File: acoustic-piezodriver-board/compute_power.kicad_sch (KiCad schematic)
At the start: 29 parts, among them J301 Conn_02x06_Odd_Even, U10 NCE6005AS, U302 TMCS1108A3UQDR, U9 LM3478MM

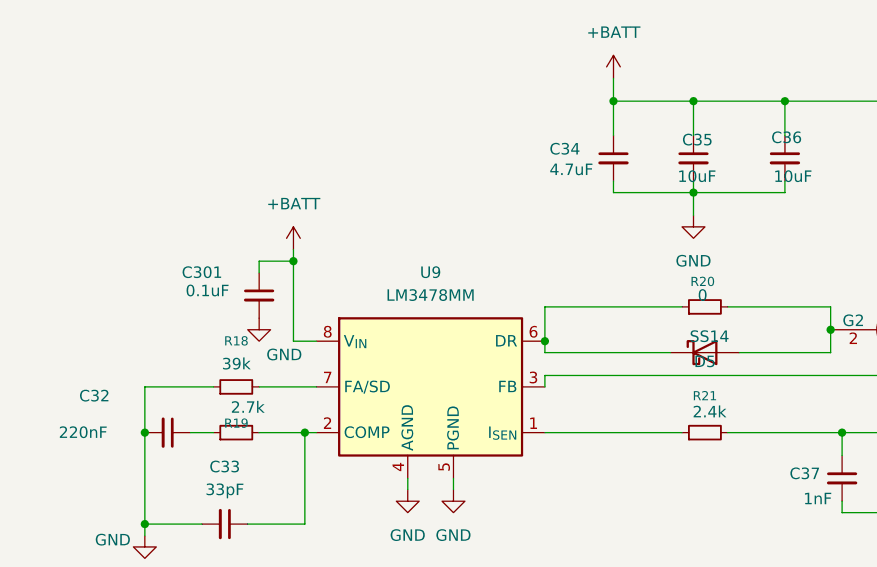
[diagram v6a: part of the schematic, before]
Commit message: Fixed ERC, DRC errors, finished routing (next) perform footprint checks
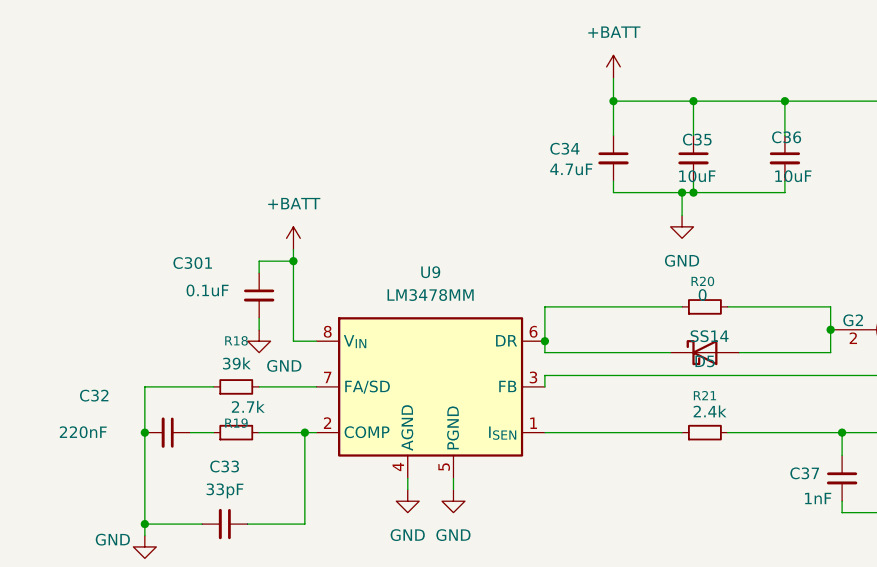
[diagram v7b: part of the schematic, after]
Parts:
- C301: footprint Capacitor_SMD:C_0201_0603Metric -> Capacitor_SMD:C_0402_1005Metric; LPN C22435929 -> C307331; MPN CGA0201X7R104K160ET -> CL05B104KB54PNC
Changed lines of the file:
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@@
 	)
 	(junction
-		(at 241.3 72.39)
+		(at 240.03 72.39)
 		(diameter 0)
 		(color 0 0 0 0)
@@
 	)
 	(junction
+		(at 241.3 72.39)
+		(diameter 0)
+		(color 0 0 0 0)
+	)
+	(junction
 		(at 50.8 62.23)
 		(diameter 0)
@@
 	(wire
 		(pts
+			(xy 193.04 87.63) (xy 193.04 86.36)
+		)
+		(stroke
+			(width 0)
+			(type default)
+		)
+	)
+	(wire
+		(pts
 			(xy 285.75 107.95) (xy 285.75 104.14)
 		)
@@
 	(wire
 		(pts
-			(xy 241.3 74.93) (xy 241.3 72.39)
+			(xy 240.03 74.93) (xy 240.03 72.39)
 		)
 		(stroke
@@
 	(wire
 		(pts
+			(xy 241.3 72.39) (xy 251.46 72.39)
+		)
+		(stroke
+			(width 0)
+			(type default)
+		)
+	)
+	(wire
+		(pts
 			(xy 45.72 140.97) (xy 45.72 135.89)
 		)
@@
 	(wire
 		(pts
-			(xy 232.41 72.39) (xy 241.3 72.39)
+			(xy 232.41 72.39) (xy 240.03 72.39)
 		)
 		(stroke
@@
 	(wire
 		(pts
-			(xy 241.3 72.39) (xy 251.46 72.39)
+			(xy 240.03 72.39) (xy 241.3 72.39)
 		)
 		(stroke
@@
 	(symbol
 		(lib_id "power:GND")
-		(at 193.04 86.36 0)
+		(at 193.04 87.63 0)
 		(unit 1)
 		(exclude_from_sim no)
@@
 		(dnp no)
 		(property "Reference" "#PWR0302"
-			(at 193.04 92.71 0)
+			(at 193.04 93.98 0)
 			(effects
 				(font
@@
 		)
 		(property "Value" "GND"
-			(at 195.834 90.424 0)
+			(at 195.834 91.694 0)
 			(effects
 				(font
@@
 		)
 		(property "Footprint" ""
-			(at 193.04 86.36 0)
+			(at 193.04 87.63 0)
 			(effects
 				(font
@@
 		)
 		(property "Datasheet" ""
-			(at 193.04 86.36 0)
+			(at 193.04 87.63 0)
 			(effects
 				(font
@@
 		)
 		(property "Description" "Power symbol creates a global label with name \"GND\" , ground"
-			(at 193.04 86.36 0)
+			(at 193.04 87.63 0)
 			(effects
 				(font
@@
 	)
 	(symbol
-		(lib_id "Device:C_Small")
-		(at 193.04 83.82 0)
-		(mirror y)
-		(unit 1)
-		(exclude_from_sim no)
-		(in_bom yes)
-		(on_board yes)
-		(dnp no)
-		(property "Reference" "C301"
-			(at 188.976 81.28 0)
-			(effects
-				(font
-					(size 1.27 1.27)
-				)
-				(justify left)
-			)
-		)
-		(property "Value" "0.1uF"
-			(at 189.738 83.312 0)
-			(effects
-				(font
-					(size 1.27 1.27)
-				)
-				(justify left)
-			)
-		)
-		(property "Footprint" "Capacitor_SMD:C_0201_0603Metric"
-			(at 193.04 83.82 0)
-			(effects
-				(font
-					(size 1.27 1.27)
-				)
-				(hide yes)
-			)
-		)
-		(property "Datasheet" "https://jlcpcb.com/api/file/downloadByFileSystemAccessId/8603345729432014848"
-			(at 193.04 83.82 0)
-			(effects
-				(font
-					(size 1.27 1.27)
-				)
-				(hide yes)
-			)
-		)
-		(property "Description" "Unpolarized capacitor, small symbol"
-			(at 193.04 83.82 0)
-			(effects
-				(font
-					(size 1.27 1.27)
-				)
-				(hide yes)
-			)
-		)
-		(property "LPN" "C22435929"
-			(at 193.04 83.82 0)
-			(effects
-				(font
-					(size 1.27 1.27)
-				)
-				(hide yes)
-			)
-		)
-		(property "MPN" "CGA0201X7R104K160ET "
-			(at 193.04 83.82 0)
-			(effects
-				(font
-					(size 1.27 1.27)
-				)
-				(hide yes)
-			)
-		)
-		(property "Availability" ""
-			(at 193.04 83.82 0)
-			(effects
-				(font
-					(size 1.27 1.27)
-				)
-				(hide yes)
-			)
-		)
-		(property "Check_prices" ""
-			(at 193.04 83.82 0)
-			(effects
-				(font
-					(size 1.27 1.27)
-				)
-				(hide yes)
-			)
-		)
-		(pin "2"
-		)
-		(pin "1"
-		)
-		(instances
-			(project "acoustic-piezodriver-board"
-				(path "/94cb090f-214e-44cc-b8ed-ae50ff29d2bf/a0fbc78d-8163-4e6b-8d81-98a3dd6573cb"
-					(reference "C301")
-					(unit 1)
-				)
-			)
-		)
-	)
-	(symbol
 		(lib_id "power:GND")
 		(at 40.64 129.54 0)
@@
 	(symbol
 		(lib_id "power:GND")
-		(at 241.3 74.93 0)
+		(at 240.03 74.93 0)
 		(unit 1)
 		(exclude_from_sim no)
@@
 		(fields_autoplaced yes)
 		(property "Reference" "#PWR042"
-			(at 241.3 81.28 0)
+			(at 240.03 81.28 0)
 			(effects
 				(font
@@
 		)
 		(property "Value" "GND"
-			(at 241.3 80.01 0)
+			(at 240.03 80.01 0)
 			(effects
 				(font
@@
 		)
 		(property "Footprint" ""
-			(at 241.3 74.93 0)
+			(at 240.03 74.93 0)
 			(effects
 				(font
@@
 		)
 		(property "Datasheet" ""
-			(at 241.3 74.93 0)
+			(at 240.03 74.93 0)
 			(effects
 				(font
@@
 		)
 		(property "Description" "Power symbol creates a global label with name \"GND\" , ground"
-			(at 241.3 74.93 0)
+			(at 240.03 74.93 0)
 			(effects
 				(font
@@
 					(unit 1)
 				)
+			)
+		)
+	)
+	(symbol
+		(lib_id "Device:C_Small")
+		(at 193.04 83.82 0)
+		(mirror y)
+		(unit 1)
+		(exclude_from_sim no)
+		(in_bom yes)
+		(on_board yes)
+		(dnp no)
+		(property "Reference" "C301"
+			(at 187.96 80.264 0)
+			(effects
+				(font
+					(size 1.27 1.27)
+				)
+				(justify left)
+			)
+		)
+		(property "Value" "0.1uF"
+			(at 189.738 83.312 0)
+			(effects
+				(font
+					(size 1.27 1.27)
+				)
+				(justify left)
+			)
+		)
+		(property "Footprint" "Capacitor_SMD:C_0402_1005Metric"
+			(at 193.04 83.82 0)
+			(effects
+				(font
+					(size 1.27 1.27)
+				)
+				(hide yes)
+			)
+		)
+		(property "Datasheet" "https://jlcpcb.com/api/file/downloadByFileSystemAccessId/8603345729432014848"
+			(at 193.04 83.82 0)
+			(effects
+				(font
+					(size 1.27 1.27)
+				)
+				(hide yes)
+			)
+		)
+		(property "Description" "Unpolarized capacitor, small symbol"
+			(at 193.04 83.82 0)
+			(effects
+				(font
+					(size 1.27 1.27)
+				)
+				(hide yes)
+			)
+		)
+		(property "LPN" "C307331"
+			(at 193.04 83.82 0)
+			(effects
+				(font
+					(size 1.27 1.27)
+				)
+				(hide yes)
+			)
+		)
+		(property "MPN" "CL05B104KB54PNC"
+			(at 193.04 83.82 0)
+			(effects
+				(font
+					(size 1.27 1.27)
+				)
+				(hide yes)
+			)
+		)
+		(pin "2"
+		)
+		(pin "1"
+		)
+		(instances
+			(project "acoustic-piezodriver-board"
+				(path "/94cb090f-214e-44cc-b8ed-ae50ff29d2bf/a0fbc78d-8163-4e6b-8d81-98a3dd6573cb"
+					(reference "C301")
+					(unit 1)
+				)

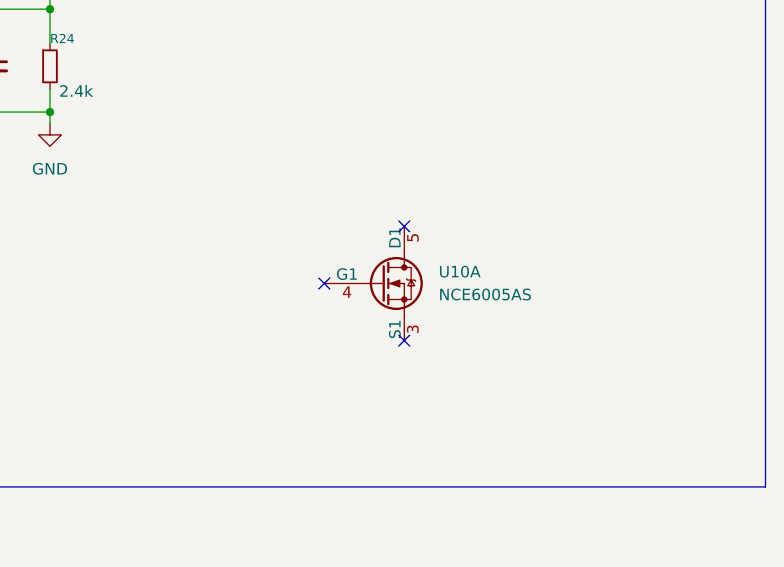
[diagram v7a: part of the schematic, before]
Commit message: changed footprints,  changed stackup from L3:PWR-> L3:GND and routed +BATT on 4th layer
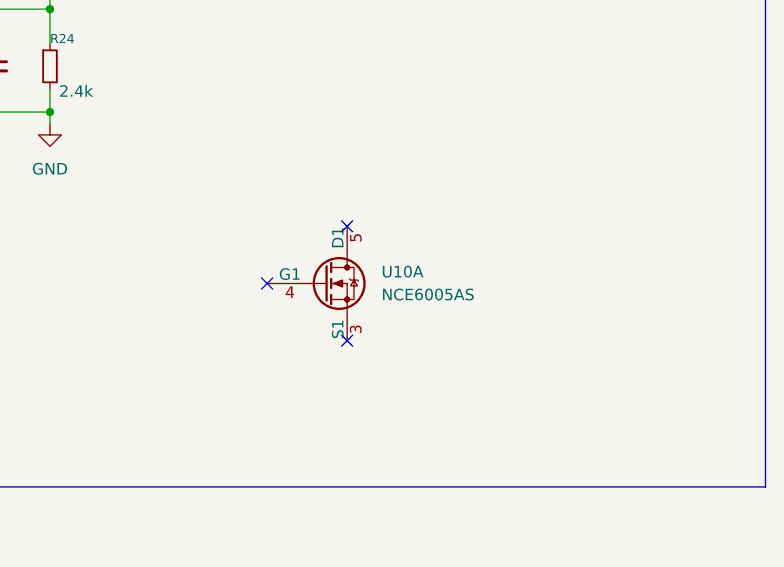
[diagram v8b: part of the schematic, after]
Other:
- moved on the sheet: U10A
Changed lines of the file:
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@@
 	)
 	(no_connect
-		(at 331.47 128.27)
+		(at 325.12 128.27)
 	)
 	(no_connect
-		(at 322.58 134.62)
+		(at 316.23 134.62)
 	)
 	(no_connect
-		(at 331.47 140.97)
+		(at 325.12 140.97)
 	)
 	(wire
@@
 	(symbol
 		(lib_id "custom_mosfet:NCE6005AS")
-		(at 331.47 134.62 0)
+		(at 325.12 134.62 0)
 		(unit 1)
 		(exclude_from_sim no)
@@
 		(fields_autoplaced yes)
 		(property "Reference" "U10"
-			(at 335.28 133.3499 0)
+			(at 328.93 133.3499 0)
 			(effects
 				(font
@@
 		)
 		(property "Value" "NCE6005AS"
-			(at 335.28 135.8899 0)
+			(at 328.93 135.8899 0)
 			(effects
 				(font
@@
 		)
 		(property "Footprint" "Package_SO:SOP-8-1EP_4.57x4.57mm_P1.27mm_EP4.57x4.45mm_ThermalVias"
-			(at 335.28 134.62 0)
+			(at 328.93 134.62 0)
 			(effects
 				(font
@@
 		)
 		(property "Datasheet" "https://jlcpcb.com/api/file/downloadByFileSystemAccessId/8588881119395647488"
-			(at 335.28 134.62 0)
+			(at 328.93 134.62 0)
 			(effects
 				(font
@@
 		)
 		(property "Description" "Dual N-channel Power MOSFET."
-			(at 331.47 134.62 0)
+			(at 325.12 134.62 0)
 			(effects
 				(font
@@
 		)
 		(property "MPN" "NCE6005AS"
-			(at 331.47 134.62 0)
+			(at 325.12 134.62 0)
 			(effects
 				(font
@@
 		)
 		(property "LPN" "C126151"
-			(at 331.47 134.62 0)
+			(at 325.12 134.62 0)
 			(effects
 				(font
